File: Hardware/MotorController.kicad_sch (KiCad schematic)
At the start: 8 parts, among them U4 STSPIN250

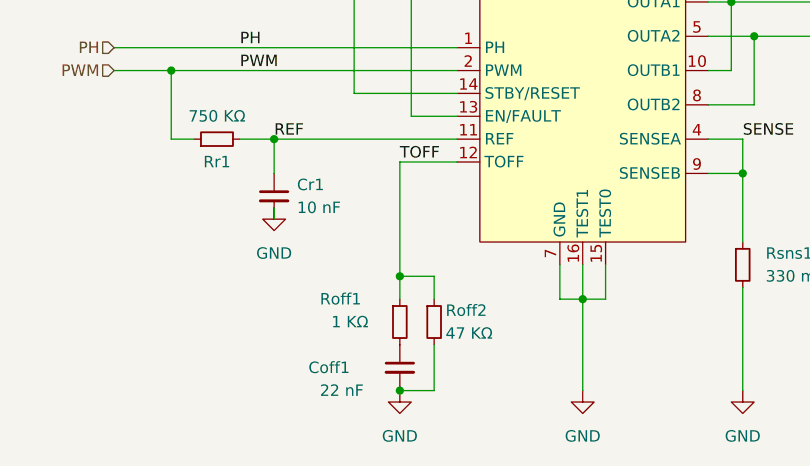
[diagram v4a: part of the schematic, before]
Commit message: Standardize I²C Bus and Route USB-C
Taking the opportunity to reroute and place STEMMA QT (JST-SH) Connectors to standardize the use of the I²C Multiplexer. Also took the chance to clean up the USB-C power supply and data line routing.
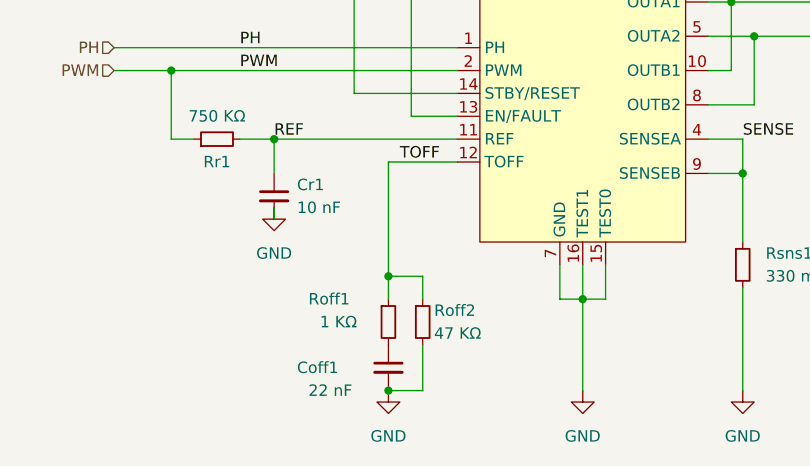
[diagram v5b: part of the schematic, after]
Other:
- moved on the sheet: Coff1, Roff1, Roff2
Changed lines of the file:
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@@
 	)
 	(junction
-		(at 128.27 144.78)
+		(at 127 144.78)
 		(diameter 0)
 		(color 0 0 0 0)
@@
 	)
 	(junction
-		(at 128.27 132.08)
+		(at 127 132.08)
 		(diameter 0)
 		(color 0 0 0 0)
@@
 	(wire
 		(pts
-			(xy 134.62 119.38) (xy 128.27 119.38)
+			(xy 134.62 119.38) (xy 127 119.38)
 		)
 		(stroke
@@
 	(wire
 		(pts
-			(xy 132.08 144.78) (xy 128.27 144.78)
+			(xy 130.81 144.78) (xy 127 144.78)
 		)
 		(stroke
@@
 	(wire
 		(pts
-			(xy 132.08 134.62) (xy 132.08 132.08)
+			(xy 130.81 134.62) (xy 130.81 132.08)
 		)
 		(stroke
@@
 	(wire
 		(pts
-			(xy 128.27 132.08) (xy 128.27 134.62)
+			(xy 127 132.08) (xy 127 134.62)
 		)
 		(stroke
@@
 	(wire
 		(pts
-			(xy 128.27 119.38) (xy 128.27 132.08)
-		)
-		(stroke
-			(width 0)
-			(type default)
-		)
-	)
-	(wire
-		(pts
-			(xy 128.27 132.08) (xy 132.08 132.08)
+			(xy 127 119.38) (xy 127 132.08)
+		)
+		(stroke
+			(width 0)
+			(type default)
+		)
+	)
+	(wire
+		(pts
+			(xy 127 132.08) (xy 130.81 132.08)
 		)
 		(stroke
@@
 	(wire
 		(pts
-			(xy 132.08 139.7) (xy 132.08 144.78)
+			(xy 130.81 139.7) (xy 130.81 144.78)
 		)
 		(stroke
@@
 	(symbol
 		(lib_id "power:GND")
-		(at 128.27 144.78 0)
+		(at 127 144.78 0)
 		(unit 1)
 		(exclude_from_sim no)
@@
 		(fields_autoplaced yes)
 		(property "Reference" "#PWR022"
-			(at 128.27 151.13 0)
+			(at 127 151.13 0)
 			(effects
 				(font
@@
 		)
 		(property "Value" "GND"
-			(at 128.27 149.86 0)
+			(at 127 149.86 0)
 			(effects
 				(font
@@
 		)
 		(property "Footprint" ""
-			(at 128.27 144.78 0)
+			(at 127 144.78 0)
 			(effects
 				(font
@@
 		)
 		(property "Datasheet" ""
-			(at 128.27 144.78 0)
+			(at 127 144.78 0)
 			(effects
 				(font
@@
 		)
 		(property "Description" ""
-			(at 128.27 144.78 0)
+			(at 127 144.78 0)
 			(effects
 				(font
@@
 	(symbol
 		(lib_id "Device:R_Small")
-		(at 132.08 137.16 0)
+		(at 130.81 137.16 0)
 		(unit 1)
 		(exclude_from_sim no)
@@
 		(dnp no)
 		(property "Reference" "Roff2"
-			(at 133.35 135.89 0)
+			(at 132.08 135.89 0)
 			(effects
 				(font
@@
 		)
 		(property "Value" "47 KΩ"
-			(at 133.35 138.43 0)
+			(at 132.08 138.43 0)
 			(effects
 				(font
@@
 		)
 		(property "Footprint" "Resistor_SMD:R_0603_1608Metric"
-			(at 132.08 137.16 0)
+			(at 130.81 137.16 0)
 			(effects
 				(font
@@
 		)
 		(property "Datasheet" "~"
-			(at 132.08 137.16 0)
+			(at 130.81 137.16 0)
 			(effects
 				(font
@@
 		)
 		(property "Description" ""
-			(at 132.08 137.16 0)
+			(at 130.81 137.16 0)
 			(effects
 				(font
@@
 	(symbol
 		(lib_id "Device:R_Small")
-		(at 128.27 137.16 0)
+		(at 127 137.16 0)
 		(unit 1)
 		(exclude_from_sim no)
@@
 		(dnp no)
 		(property "Reference" "Roff1"
-			(at 119.38 134.62 0)
+			(at 118.11 134.62 0)
 			(effects
 				(font
@@
 		)
 		(property "Value" "1 KΩ"
-			(at 120.65 137.16 0)
+			(at 119.38 137.16 0)
 			(effects
 				(font
@@
 		)
 		(property "Footprint" "Resistor_SMD:R_0603_1608Metric"
-			(at 128.27 137.16 0)
+			(at 127 137.16 0)
 			(effects
 				(font
@@
 		)
 		(property "Datasheet" "~"
-			(at 128.27 137.16 0)
+			(at 127 137.16 0)
 			(effects
 				(font
@@
 		)
 		(property "Description" ""
-			(at 128.27 137.16 0)
+			(at 127 137.16 0)
 			(effects
 				(font
@@
 	(symbol
 		(lib_id "Device:C_Small")
-		(at 128.27 142.24 0)
+		(at 127 142.24 0)
 		(unit 1)
 		(exclude_from_sim no)
@@
 		(dnp no)
 		(property "Reference" "Coff1"
-			(at 118.11 142.24 0)
+			(at 116.84 142.24 0)
 			(effects
 				(font
@@
 		)
 		(property "Value" "22 nF"
-			(at 119.38 144.78 0)
+			(at 118.11 144.78 0)
 			(effects
 				(font
@@
 		)
 		(property "Footprint" "Capacitor_SMD:C_0603_1608Metric"
-			(at 128.27 142.24 0)
+			(at 127 142.24 0)
 			(effects
 				(font
@@
 		)
 		(property "Datasheet" "~"
-			(at 128.27 142.24 0)
+			(at 127 142.24 0)
 			(effects
 				(font
@@
 		)
 		(property "Description" ""
-			(at 128.27 142.24 0)
-			(effects
-				(font
+			(at 127 142.24 0)
+			(effects
+				(font
